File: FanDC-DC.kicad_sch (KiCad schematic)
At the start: 19 parts, among them IC3 TPS56A37RPAR, J3 Conn_01x02, Q3 2N7002_SOT-23-3

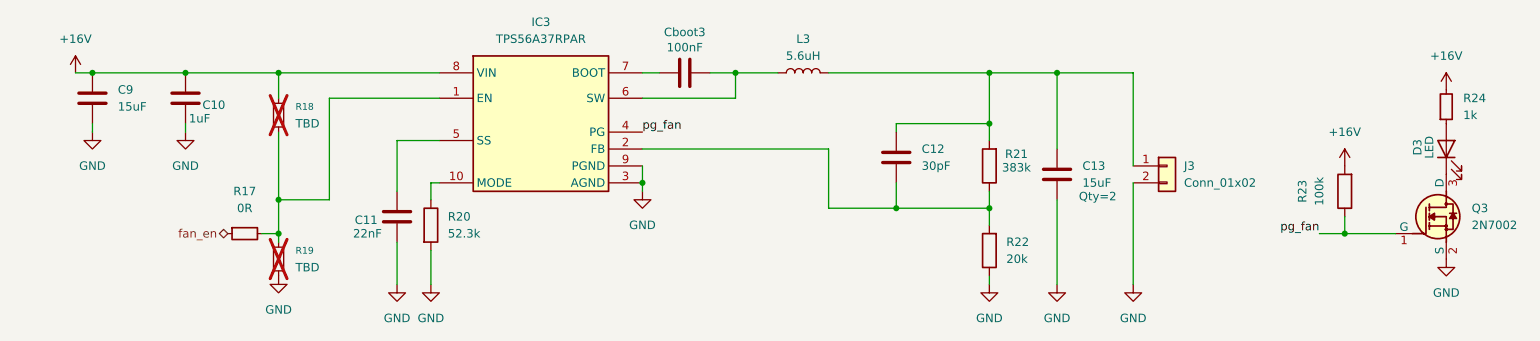
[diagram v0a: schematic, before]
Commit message: Minimal version without BMS
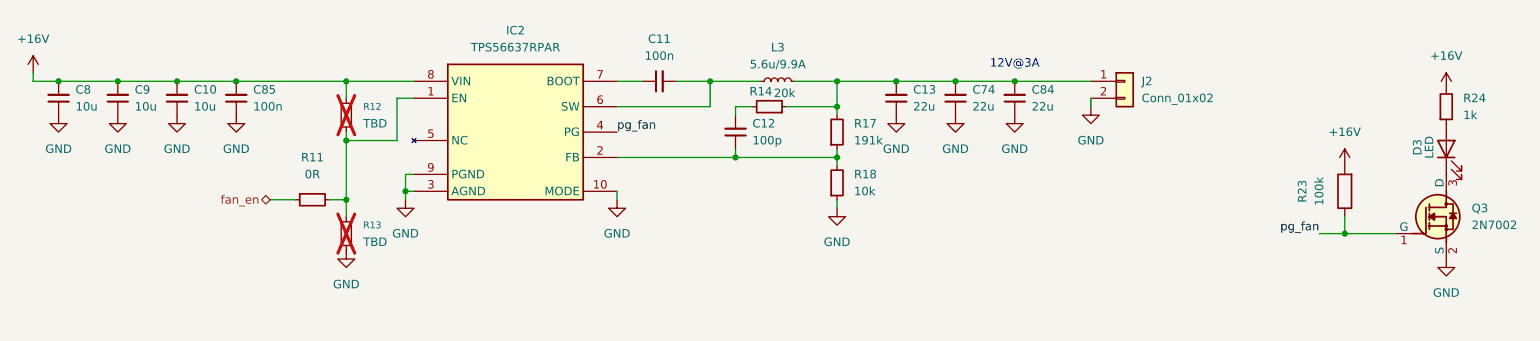
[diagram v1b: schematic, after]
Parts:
- removed C10: 1uF, symbol lib:C
- removed C11: 22nF, symbol lib:C
- removed C12: 30pF, symbol lib:C
- removed C13, C9: 15uF, symbol lib:C
- removed Cboot3: 100nF, symbol lib:C
- removed IC3: TPS56A37RPAR, TPS56A37RPAR, symbol lib:TPS56A37RPAR
- removed J3: Conn_01x02, symbol lib:Conn_01x02
- removed L3: 5.6uH, symbol lib:L
- removed R17: R_0R_0402, Hardware Components Footprints:R_0402_1005Metric, symbol lib:R_0R_0402
- removed R18, R19: TBD, symbol lib:R_Small
- removed R20: 52.3k, symbol lib:R
- removed R21: 383k, symbol lib:R
- removed R22: 20k, symbol lib:R
- added C10, C8, C9: C_10u_1206, Hardware Components Footprints:C_1206_3216Metric, symbol Hardware Components:C_10u_1206
- added C11, C85: C_100n_16V_X7R_0402, Hardware Components Footprints:C_0402_1005Metric, symbol Hardware Components:C_100n_16V_X7R_0402
- added C12: C_100p_0402, Hardware Components Footprints:C_0402_1005Metric, symbol Hardware Components:C_100p_0402
- added C13, C74, C84: C_22u_25V_X7R_1210, Hardware Components Footprints:C_1210_3225Metric, symbol Hardware Components:C_22u_25V_X7R_1210
- added IC2: TPS56637RPAR, TPS56637RPAR, symbol lib:TPS56637RPAR_1
- added J2: Conn_01x02, TerminalBlock_Phoenix:TerminalBlock_Phoenix_MKDS-1,5-2-5.08_1x02_P5.08mm_Horizontal, symbol lib:Conn_01x02
- added L3: L_4u7_11A_Coilcraft-XAL6060, Hardware Components Footprints:L_Coilcraft-XAL6060, symbol Hardware Components:L_4u7_11A_Coilcraft-XAL6060
- added R11: R_0R_0402, Hardware Components Footprints:R_0402_1005Metric, symbol lib:R_0R_0402
- added R12, R13: TBD, Hardware Components Footprints:R_0402_1005Metric, symbol lib:R_Small
- added R14: R_20k_0402, Hardware Components Footprints:R_0402_1005Metric, symbol Hardware Components:R_20k_0402
- added R17: R_191k_0402, Hardware Components Footprints:R_0402_1005Metric, symbol Hardware Components:R_191k_0402
- added R18: R_10k_0402, Hardware Components Footprints:R_0402_1005Metric, symbol lib:R_10k_0402
- D3: footprint (none) -> LED_SMD:LED_0603_1608Metric
- R23: footprint (none) -> Hardware Components Footprints:R_0402_1005Metric
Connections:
- net +16V: now also C10.2, C8.2, C85.2, C9.2, IC2.8 (VIN), R12.1
- net GND: now also C10.1, C13.1, C74.1, C8.1, C84.1, C85.1, C9.1, IC2.10 (MODE), IC2.3 (AGND), IC2.9 (PGND), J2.2 (Pin_2), R13.2, R18.1
- net fan_en : now also R11.1
- net pg_fan: now also IC2.4 (PG)
- new net: IC2.1 (EN), R11.2, R12.2, R13.1
- new net: C13.2, C74.2, C84.2, J2.1 (Pin_1), L3.2, R14.1, R17.2
- new net: C12.2, R14.2
- new net: C11.2, IC2.6 (SW), L3.1
- new net: C12.1, IC2.2 (FB), R17.1, R18.2
- new net: C11.1, IC2.7 (BOOT)
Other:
- note added: "12V@3A"
